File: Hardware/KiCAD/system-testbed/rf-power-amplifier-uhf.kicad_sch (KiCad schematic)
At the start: 22 parts, among them U8 GRF5604

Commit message: feat: assign 0603 passive component footprints #32 #34
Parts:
- C23, C25, C26, C31, C32, C38, C55, C56, C57, C58, C59, C60, C62: footprint (none) -> Capacitor_SMD:C_0603_1608Metric
- L12, L13, L14: footprint (none) -> Inductor_SMD:L_0603_1608Metric
- L39: renamed from C39; footprint (none) -> Inductor_SMD:L_0603_1608Metric
- R14, R3, R6: footprint (none) -> Resistor_SMD:R_0603_1608Metric
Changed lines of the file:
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@@
 			)
 		)
-		(property "Footprint" ""
+		(property "Footprint" "Resistor_SMD:R_0603_1608Metric"
 			(at 26.924 36.576 90)
 			(effects
@@
 			)
 		)
-		(property "Footprint" ""
+		(property "Footprint" "Capacitor_SMD:C_0603_1608Metric"
 			(at 142.24 87.63 0)
 			(effects
@@
 		(dnp no)
 		(fields_autoplaced yes)
-		(property "Reference" "C39"
+		(property "Reference" "L39"
 			(at 113.03 76.2 90)
 			(effects
@@
 			)
 		)
-		(property "Footprint" ""
+		(property "Footprint" "Inductor_SMD:L_0603_1608Metric"
 			(at 113.03 81.28 0)
 			(effects
@@
 			(project "system-testbed"
 				(path "/72756aea-0ff9-4757-9699-8d0f18588f6f/663959ae-8fbf-4d79-b07e-771da73defb9/3a0c59ed-a639-4c21-bd1b-b48b5d30f73c/dae276e1-5582-4059-9e99-48b7cafef9a9"
-					(reference "C39")
+					(reference "L39")
 					(unit 1)
 				)
@@
 			)
 		)
-		(property "Footprint" ""
+		(property "Footprint" "Capacitor_SMD:C_0603_1608Metric"
 			(at 119.38 87.63 0)
 			(effects
@@
 			)
 		)
-		(property "Footprint" ""
+		(property "Footprint" "Capacitor_SMD:C_0603_1608Metric"
 			(at 41.91 81.28 0)
 			(effects
@@
 			)
 		)
-		(property "Footprint" ""
+		(property "Footprint" "Capacitor_SMD:C_0603_1608Metric"
 			(at 58.42 49.53 0)
 			(effects
@@
 			)
 		)
-		(property "Footprint" ""
+		(property "Footprint" "Capacitor_SMD:C_0603_1608Metric"
 			(at 153.67 87.63 0)
 			(effects
@@
 			)
 		)
-		(property "Footprint" ""
+		(property "Footprint" "Resistor_SMD:R_0603_1608Metric"
 			(at 42.164 36.576 90)
 			(effects
@@
 			)
 		)
-		(property "Footprint" ""
+		(property "Footprint" "Capacitor_SMD:C_0603_1608Metric"
 			(at 125.73 46.99 0)
 			(effects
@@
 			)
 		)
-		(property "Footprint" ""
+		(property "Footprint" "Capacitor_SMD:C_0603_1608Metric"
 			(at 115.57 46.99 0)
 			(effects
@@
 			)
 		)
-		(property "Footprint" ""
+		(property "Footprint" "Resistor_SMD:R_0603_1608Metric"
 			(at 92.964 67.564 90)
 			(effects
@@
 			)
 		)
-		(property "Footprint" ""
+		(property "Footprint" "Inductor_SMD:L_0603_1608Metric"
 			(at 25.4 87.63 0)
 			(effects
@@
 			)
 		)
-		(property "Footprint" ""
+		(property "Footprint" "Capacitor_SMD:C_0603_1608Metric"
 			(at 160.02 81.28 0)
 			(effects
@@
 			)
 		)
-		(property "Footprint" ""
+		(property "Footprint" "Capacitor_SMD:C_0603_1608Metric"
 			(at 27.94 49.53 0)
 			(effects
@@
 			)
 		)
-		(property "Footprint" ""
+		(property "Footprint" "Capacitor_SMD:C_0603_1608Metric"
 			(at 99.06 87.63 0)
 			(effects
@@
 			)
 		)
-		(property "Footprint" ""
+		(property "Footprint" "Inductor_SMD:L_0603_1608Metric"
 			(at 68.58 49.53 0)
 			(effects
@@
 			)
 		)
-		(property "Footprint" ""
+		(property "Footprint" "Capacitor_SMD:C_0603_1608Metric"
 			(at 130.81 87.63 0)
 			(effects
@@
 			)
 		)
-		(property "Footprint" ""
+		(property "Footprint" "Inductor_SMD:L_0603_1608Metric"
 			(at 99.06 74.93 0)
 			(effects
@@
 			)
 		)
-		(property "Footprint" ""
+		(property "Footprint" "Capacitor_SMD:C_0603_1608Metric"
 			(at 43.18 49.53 0)
 			(effects
@@
 			)
 		)
-		(property "Footprint" ""
+		(property "Footprint" "Capacitor_SMD:C_0603_1608Metric"
 			(at 31.75 81.28 0)
 			(effects

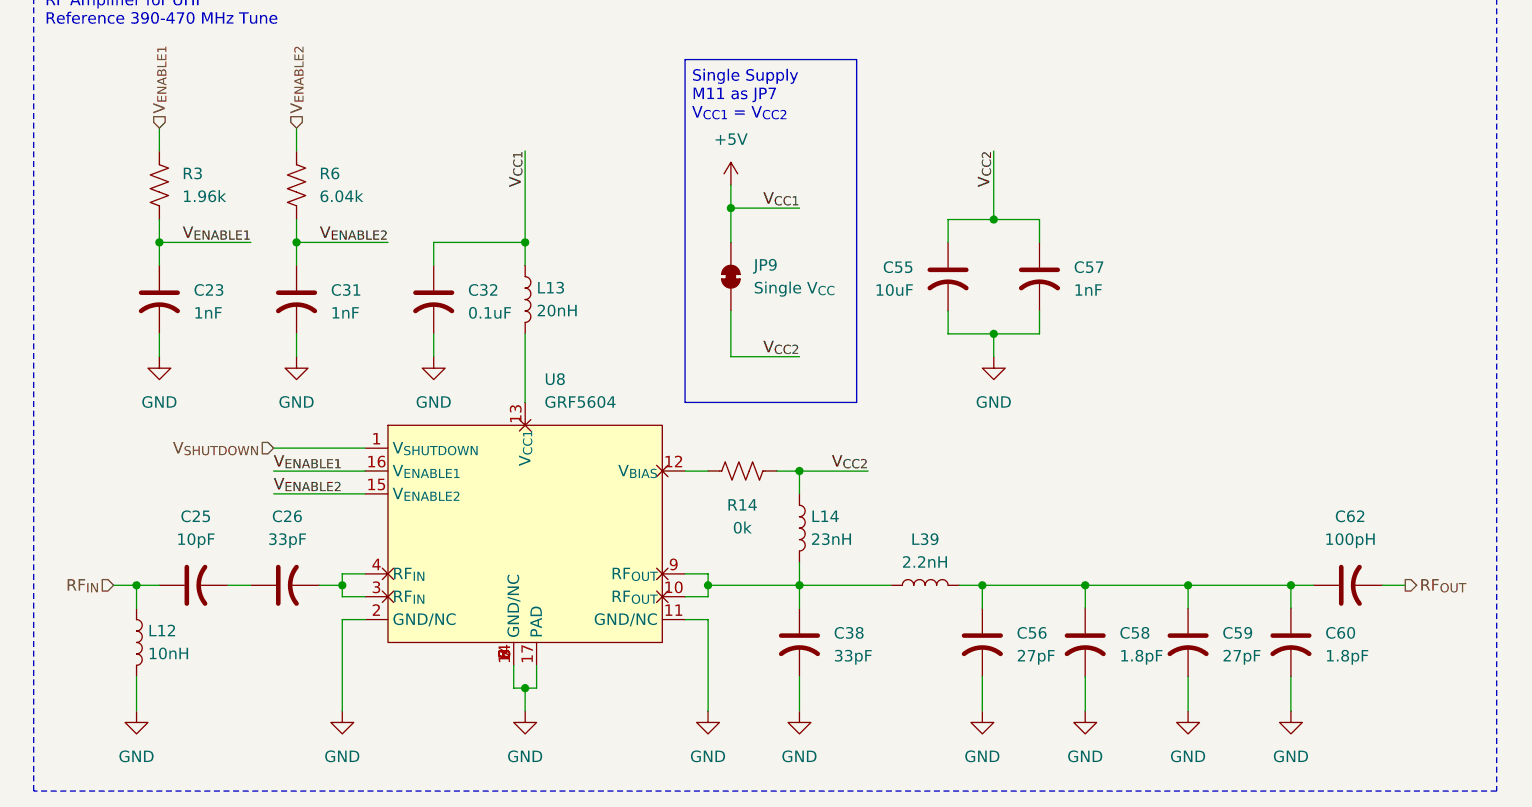
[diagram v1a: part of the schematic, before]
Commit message: fix: import RF sheet contents #65
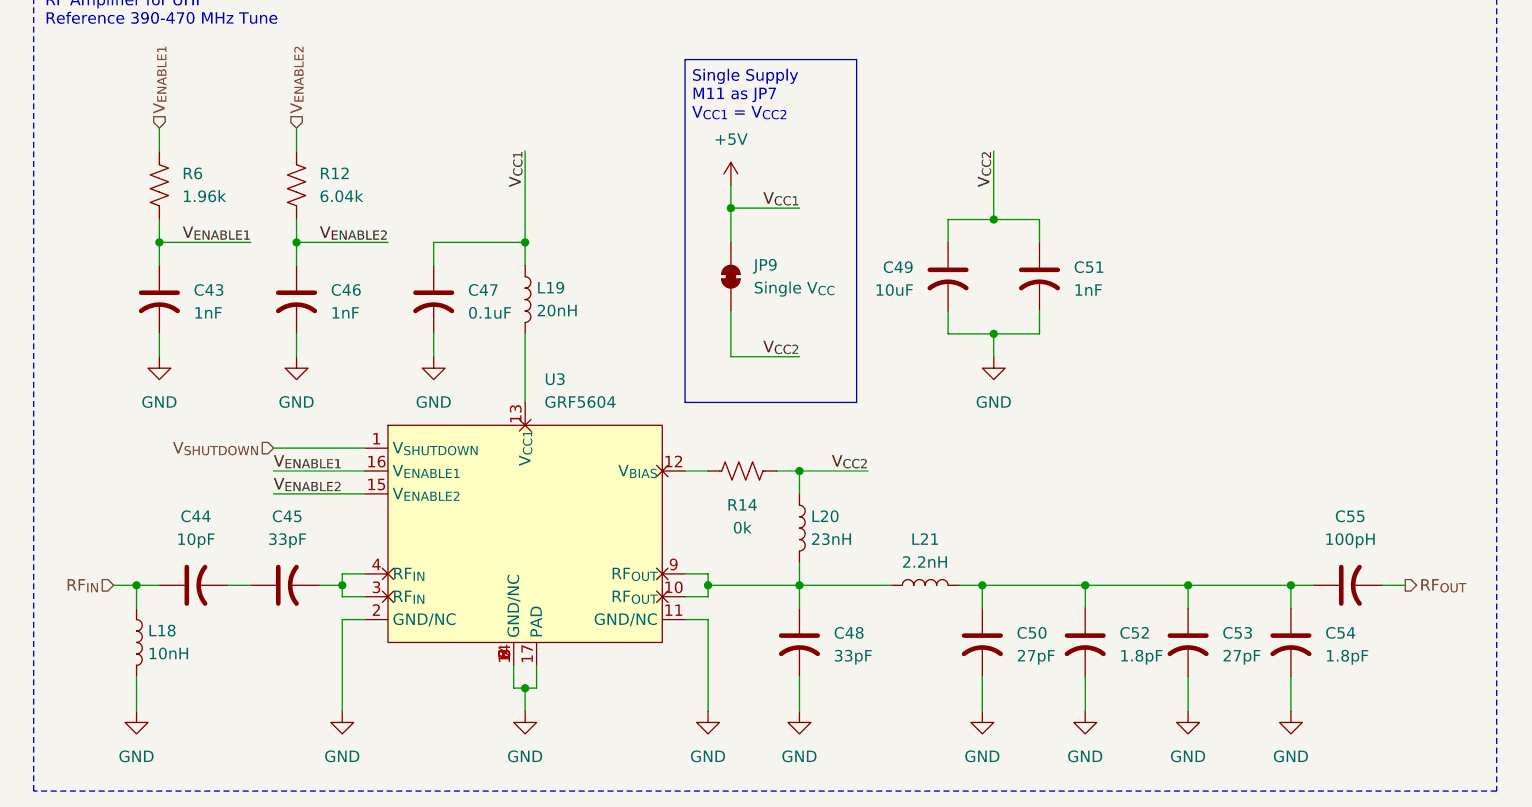
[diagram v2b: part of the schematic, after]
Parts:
- renumbered C23 to C43, C25 to C44, C26 to C45, C31 to C46, C32 to C47, C38 to C48, C55 to C49, C56 to C50, C57 to C51, C58 to C52, C59 to C53, C60 to C54, C62 to C55, L12 to L18, L13 to L19, L14 to L20, L39 to L21, R6 to R12, R3 to R6, U8 to U3

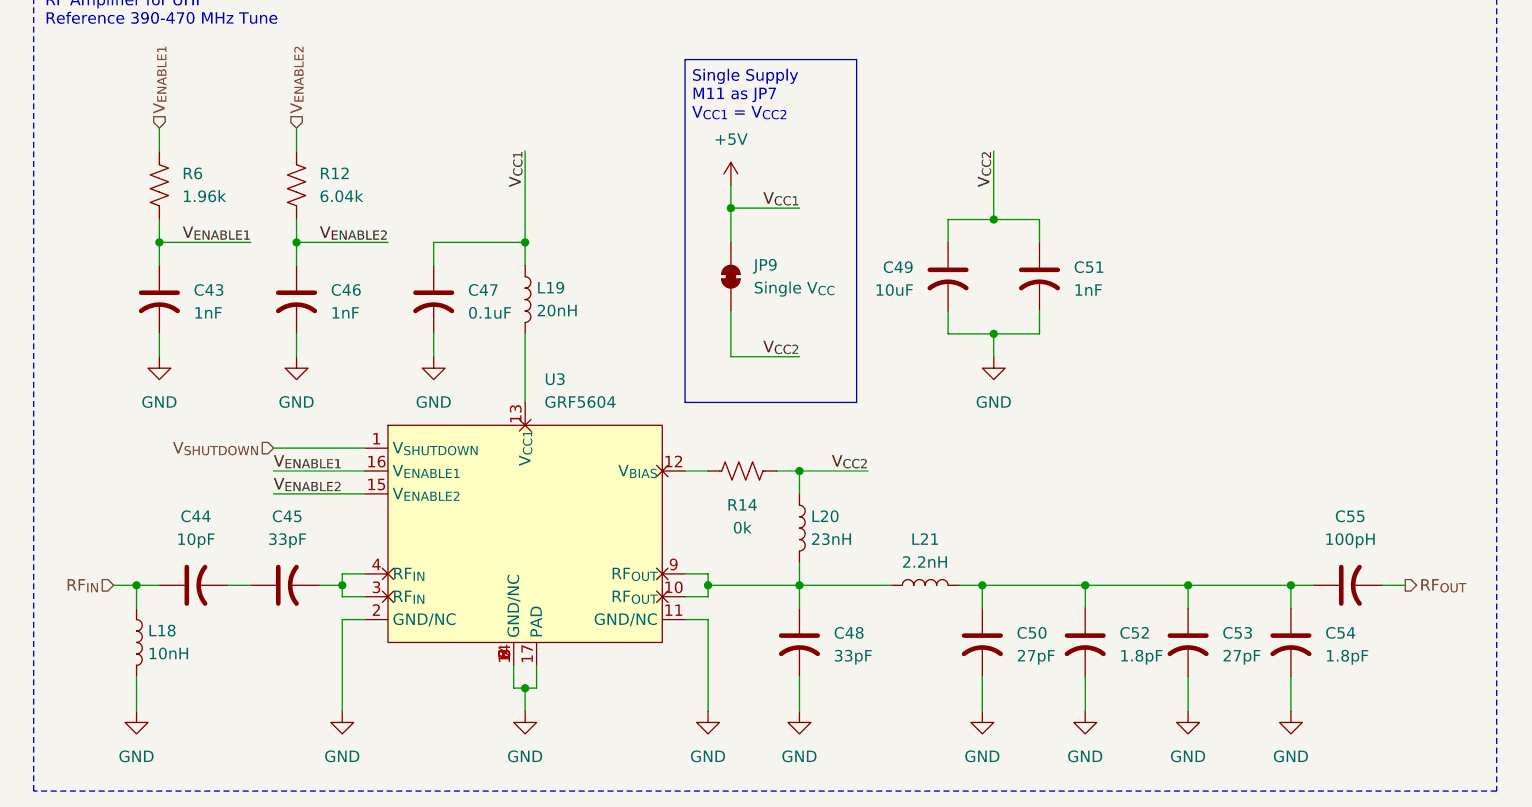
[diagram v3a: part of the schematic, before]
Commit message: fix: reannotate schematics for pcb editor use #55
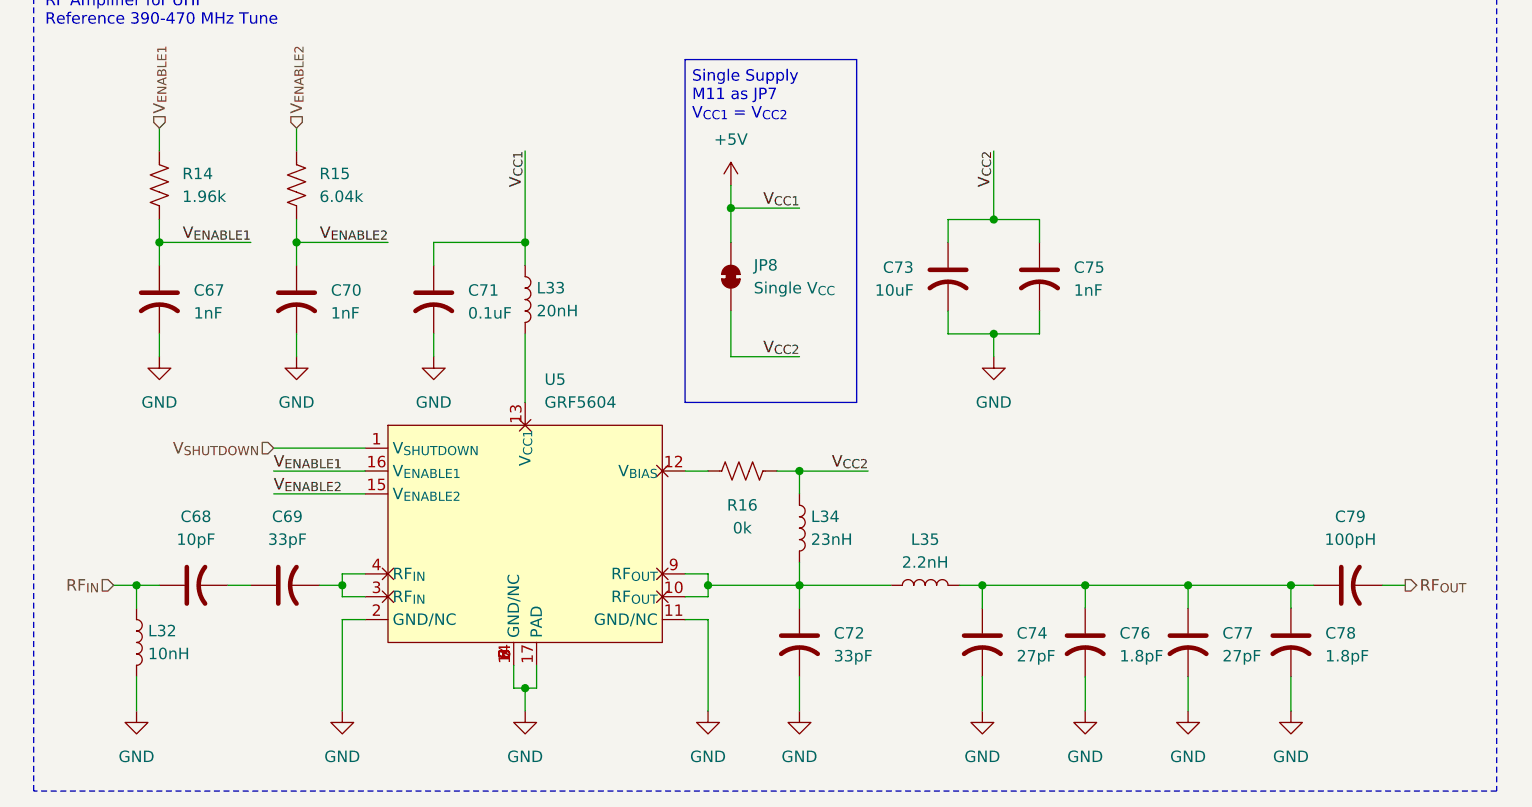
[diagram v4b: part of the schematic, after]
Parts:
- L32: renamed from L18; footprint Inductor_SMD:L_0603_1608Metric -> Inductor_SMD:L_0402_1005Metric
- L33: renamed from L19; footprint Inductor_SMD:L_0603_1608Metric -> Inductor_SMD:L_0402_1005Metric
- L34: renamed from L20; footprint Inductor_SMD:L_0603_1608Metric -> Inductor_SMD:L_0402_1005Metric
- L35: renamed from L21; footprint Inductor_SMD:L_0603_1608Metric -> Inductor_SMD:L_0402_1005Metric
- renumbered C43 to C67, C44 to C68, C45 to C69, C46 to C70, C47 to C71, C48 to C72, C49 to C73, C50 to C74, C51 to C75, C52 to C76, C53 to C77, C54 to C78, C55 to C79, JP9 to JP8, R6 to R14, R12 to R15, R14 to R16, U3 to U5

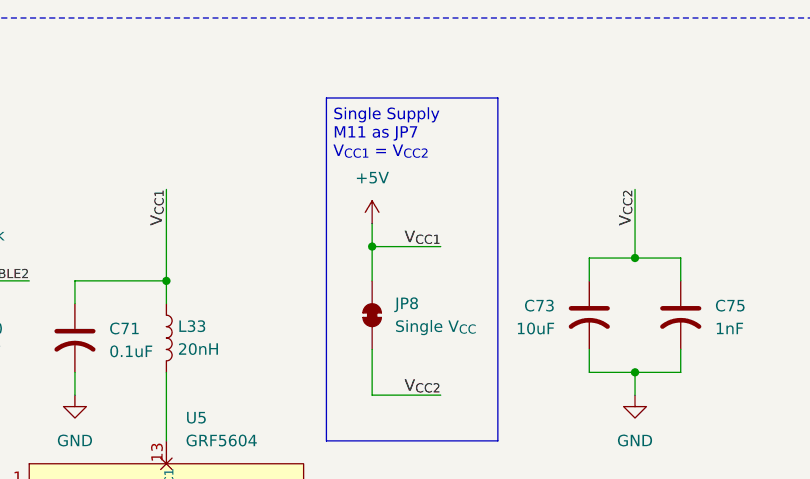
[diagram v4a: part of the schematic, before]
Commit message: fix: allow for DRC use in PCB editor by successful reannotation
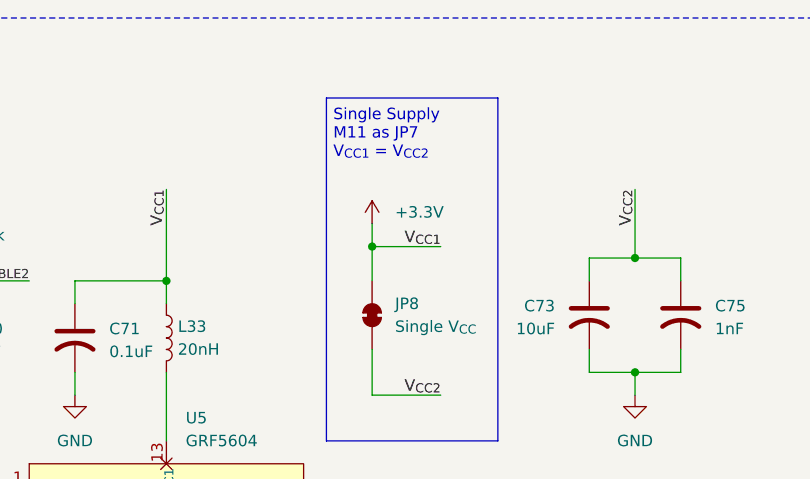
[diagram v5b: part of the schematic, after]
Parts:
- C67, C68, C69, C70, C71, C72, C73, C74, C75, C76, C77, C78, C79: footprint Capacitor_SMD:C_0603_1608Metric -> Capacitor_SMD:C_0402_1005Metric
- R14, R15, R16: footprint Resistor_SMD:R_0603_1608Metric -> Resistor_SMD:R_0402_1005Metric
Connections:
- net +5V renamed +3.3V
